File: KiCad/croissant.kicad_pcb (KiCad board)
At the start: 2 copper layers, 149.8 x 90.3 mm, 54 parts, among them J1 USB_C_Receptacle_PowerOnly_6P, Q1 NMOS, SW1 SW_SPDT, U1 NE556, U2 TL064

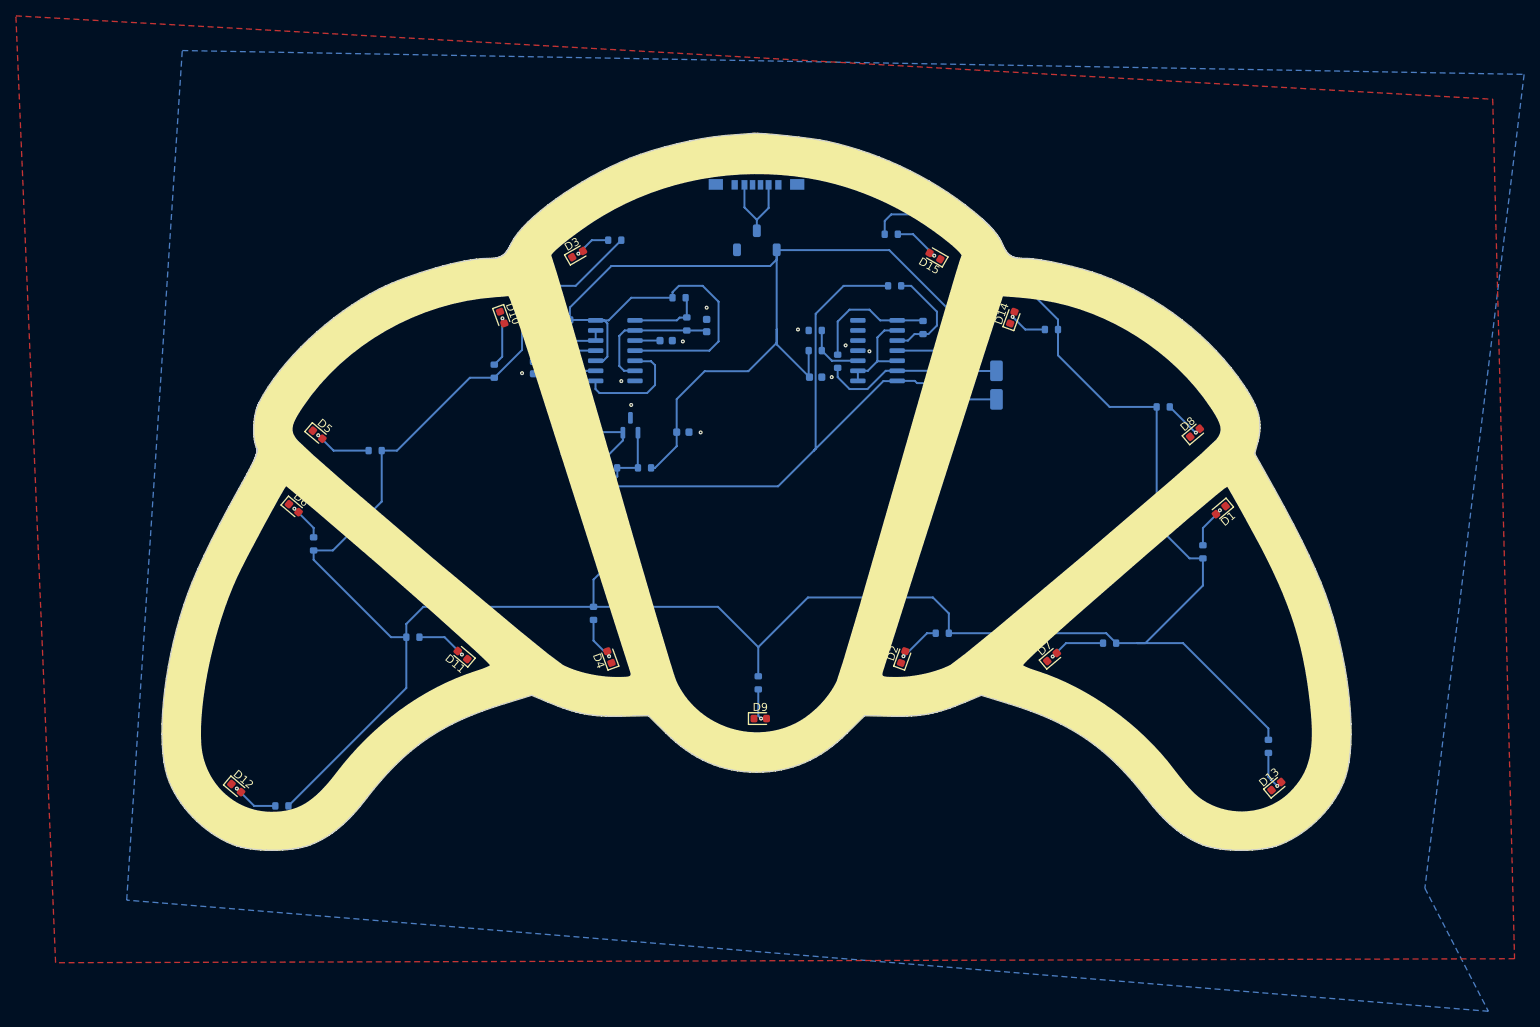
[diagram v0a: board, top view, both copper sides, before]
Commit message: Fix LEDs silkscreen
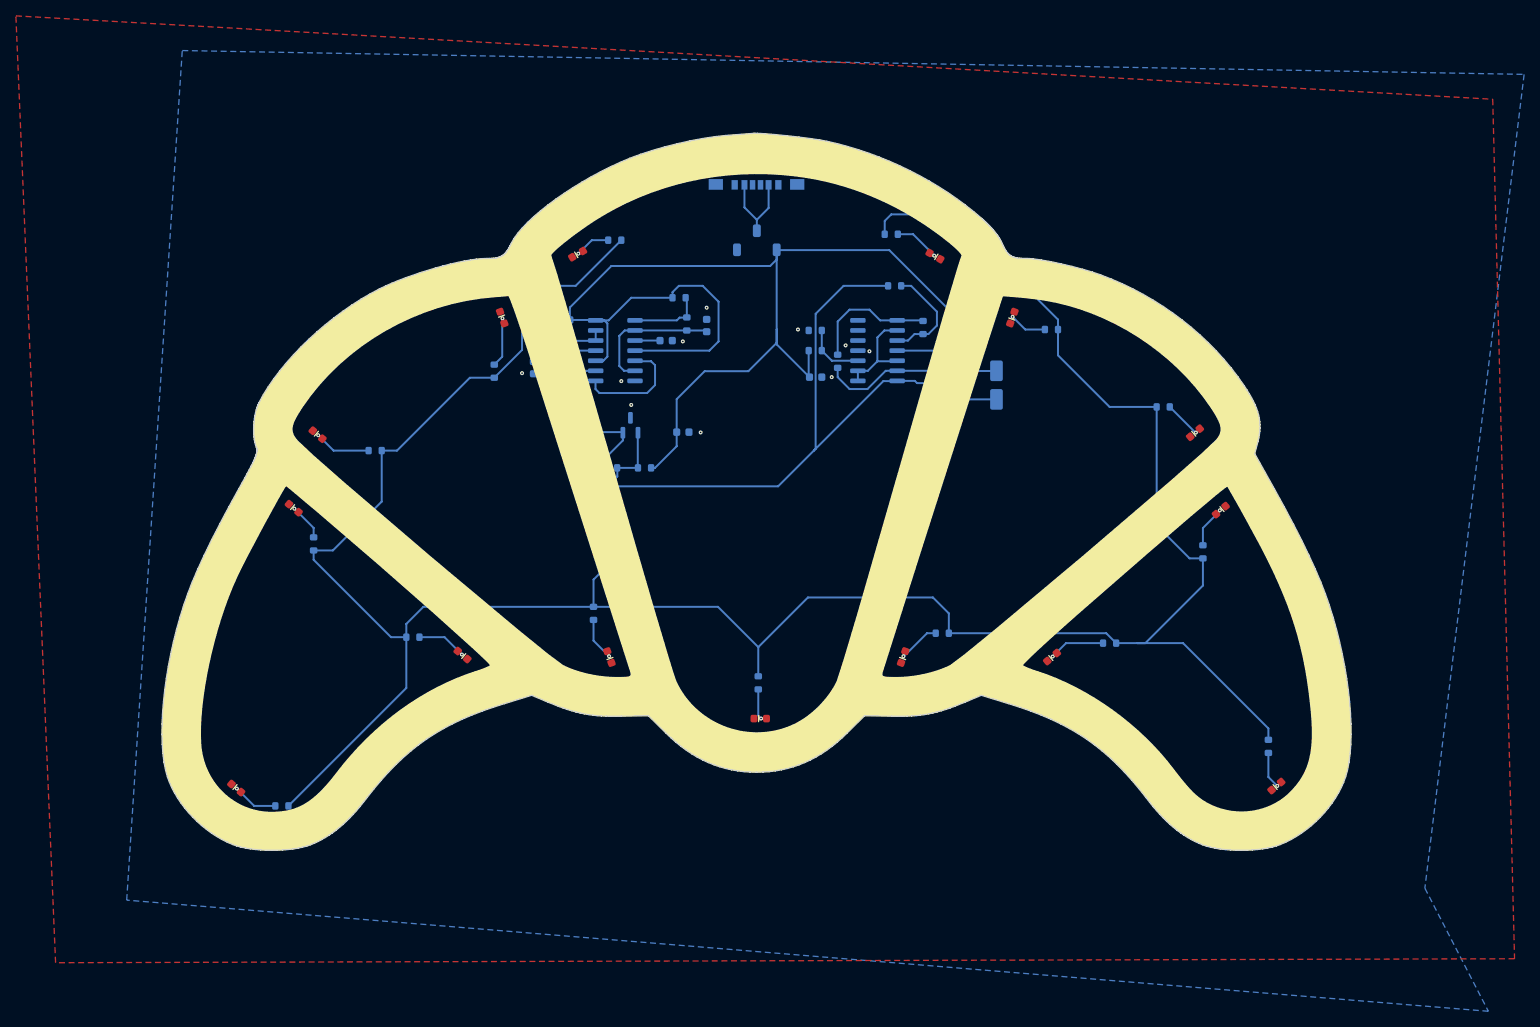
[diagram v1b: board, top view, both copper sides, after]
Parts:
- D1, D10, D11, D12, D13, D14, D15, D2, D3, D4, D5, D6, D7, D8, D9: footprint LED_SMD:LED_0603_1608Metric -> croissant:LED_0603_NOSILK
